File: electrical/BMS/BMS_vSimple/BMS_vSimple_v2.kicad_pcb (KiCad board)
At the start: 4 copper layers, 109 x 52.9 mm, 145 parts, among them J1 Conn_01x04_Pin, J2 Conn_01x13_Socket, J3 Conn_01x13_Socket, Q6 BCP56, U1 STM32F412RGTx, U2 BQ79652PAPRQ1, U3 ISO1044BD, U4 CD74HC4067M

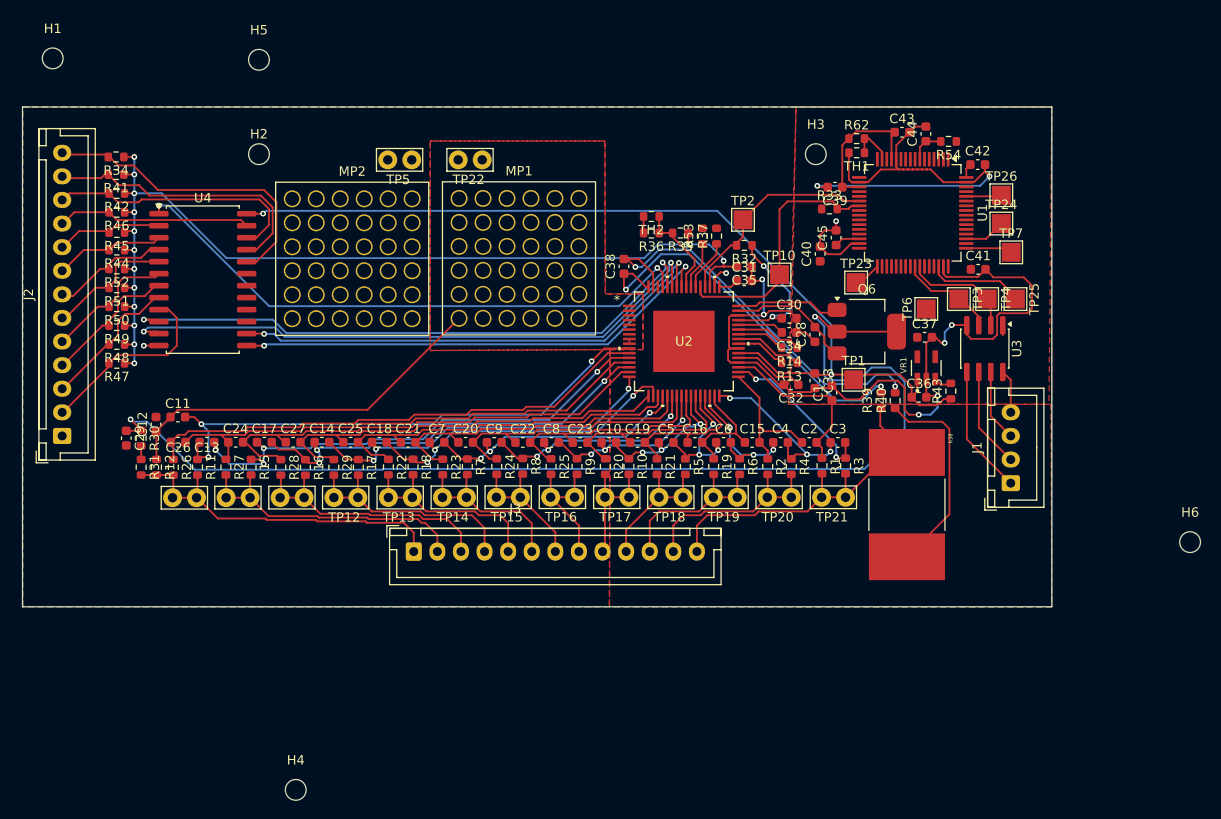
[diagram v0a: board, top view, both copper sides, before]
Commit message: revised BMS, ty Joseph for feedback :D
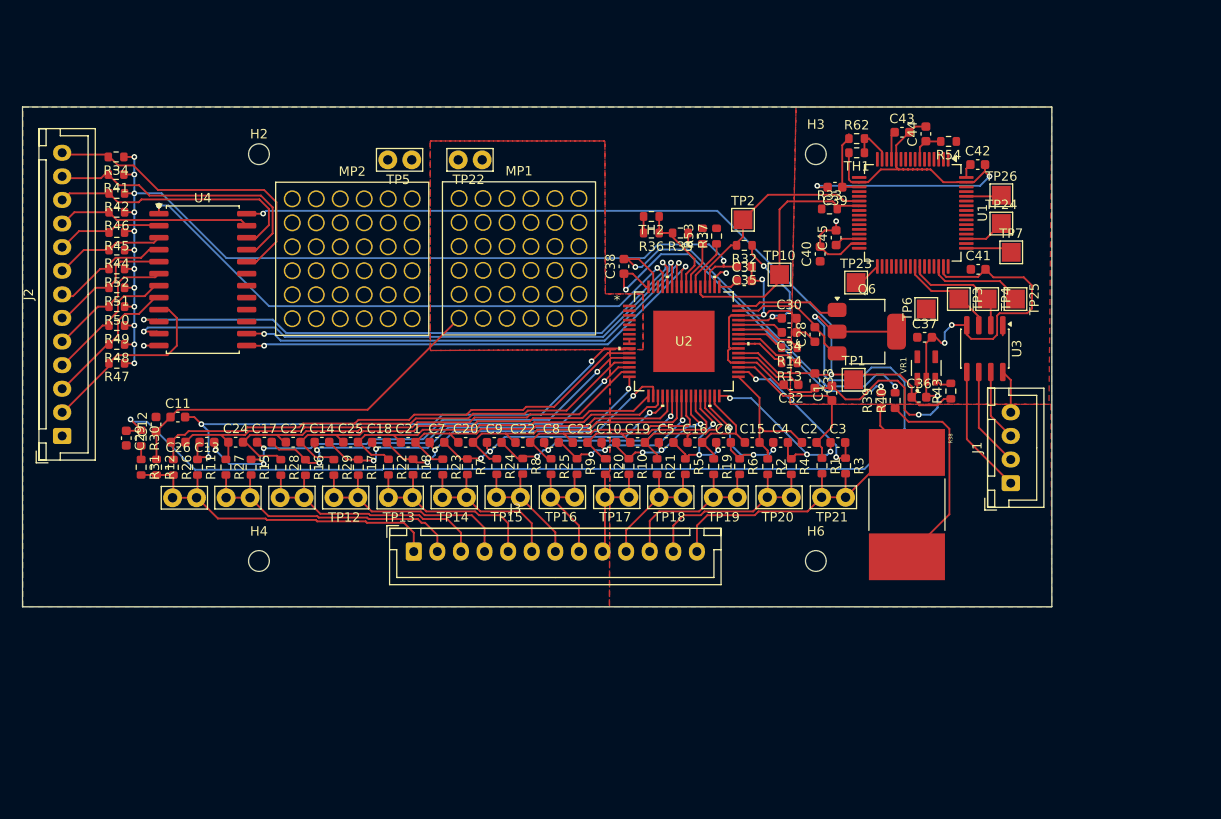
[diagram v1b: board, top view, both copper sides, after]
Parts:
- removed H1, H5: MountingHole, MountingHole:MountingHole_2.2mm_M2
- moved H6 39.7 mm to (115.6, 121.0)
- moved H4 24.6 mm to (56.6, 121.0)
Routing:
- net /VDD1: track 18.6 -> 13.5 mm
- net /SRP: track 41.2 -> 40.4 mm
